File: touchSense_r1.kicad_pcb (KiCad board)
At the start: 2 copper layers, 25 x 25 mm, 13 parts, among them J101 breakout, J102 GS2, J103 GS3, J104 cap/daisy, J105 GS2, U101 AT42QT1010-TSHR

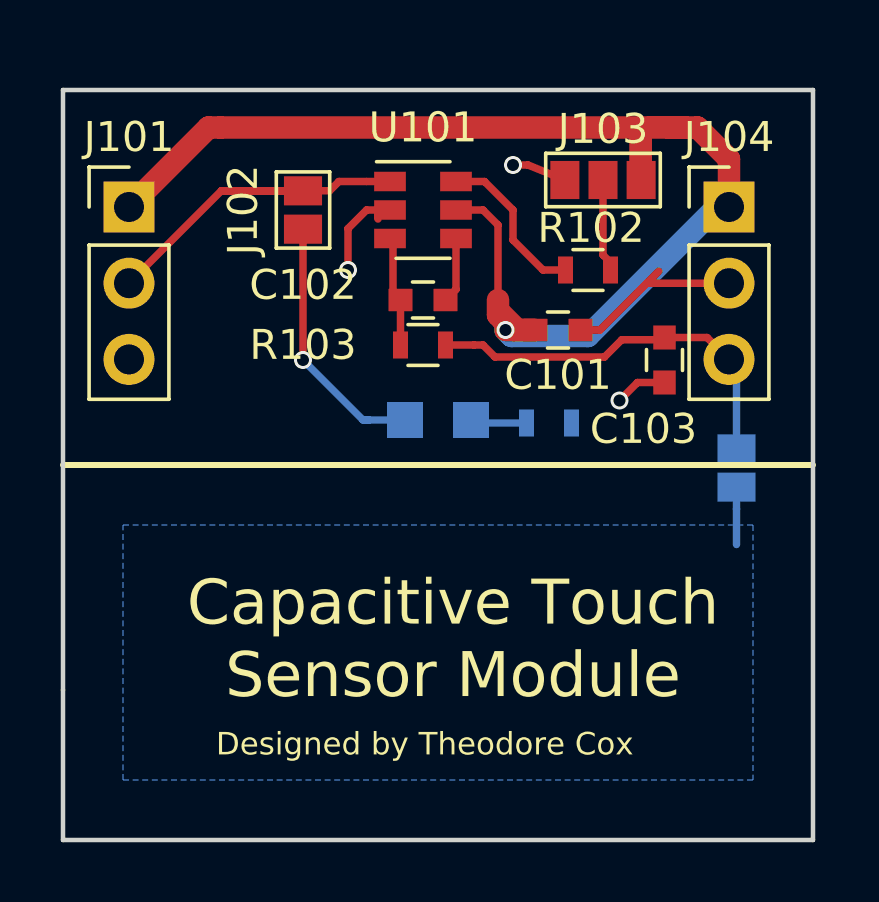
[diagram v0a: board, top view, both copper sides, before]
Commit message: finalized pcblayouts, before uploading to manufacturer
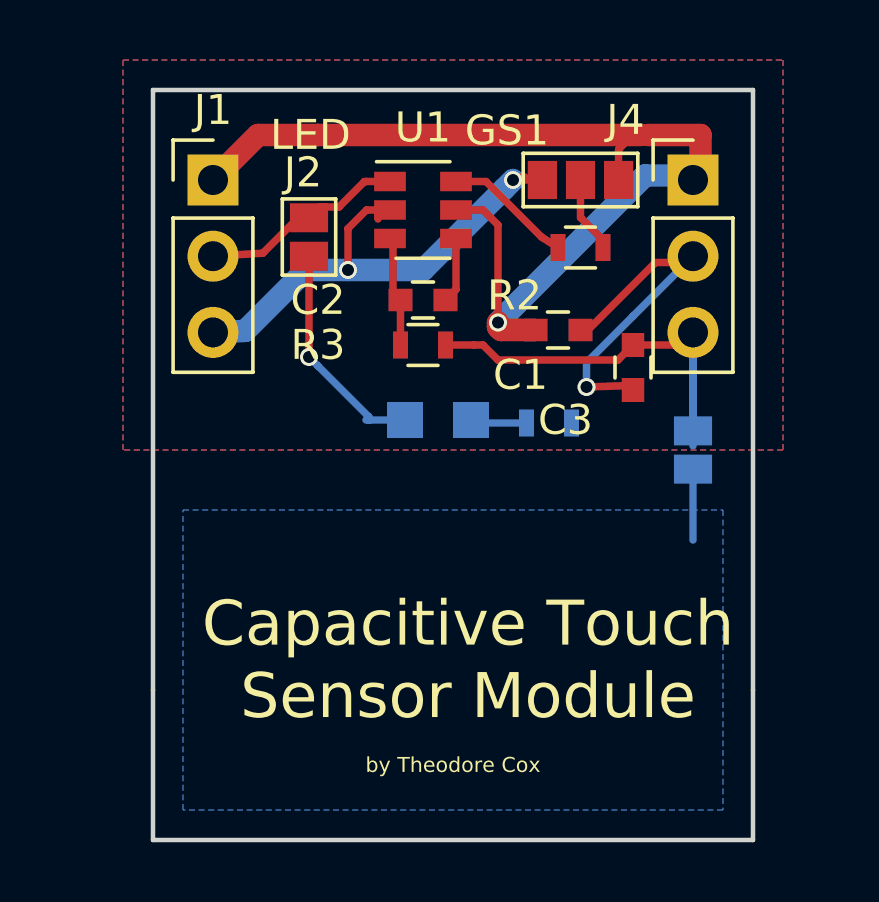
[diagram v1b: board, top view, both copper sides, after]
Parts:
- removed J103: GS3, Connectors:GS3
- added GS1: GS3, Connectors:GS3, F.Cu at (117.2, 103.0)
- added REF***: OSHW-Symbol_13.4x12mm_SilkScreen, Symbols:OSHW-Symbol_13.4x12mm_SilkScreen, B.Cu at (113.0, 119.0)
- moved J1 2.94 mm to (105.0, 103.0)
- moved J3 1.57 mm to (121.0, 112.0)
- moved J4 1.50 mm to (121.0, 103.0)
- moved C3 1.08 mm to (119.0, 109.2)
- moved J2 0.92 mm to (108.2, 104.9)
- moved R2 0.79 mm to (117.2, 105.2)
- renumbered C101 to C1, C102 to C2, C103 to C3, D101 to D1, J101 to J1, J102 to J2, J105 to J3, J104 to J4, R101 to R1, R102 to R2, R103 to R3, U101 to U1
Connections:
- J3 pad 2: (no net) -> /internal
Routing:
- net GND: track 13.9 -> 29.5 mm
- net /VDD: track 48.0 -> 37.6 mm
- net /OUT1: track 14.9 -> 7.88 mm
- net /internal: track 0.00 -> 2.36 mm
- net /CAP_PAD: track 14.2 -> 16.4 mm
- net (no net): track 1.91 -> 0.00 mm
- net Net-(R2-Pad2): track 5.46 -> 4.27 mm
- net Net-(D1-Pad2): track 9.40 -> 8.30 mm
- net Net-(GS1-Pad2): track 3.10 -> 2.56 mm
- added copper zone on B.Cu, net /internal
- removed copper zone on B.Cu, net /CAP_PAD
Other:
- board size 25 x 25 mm -> 20 x 25 mm
- board text added: "LED"
- board text added: "by Theodore Cox"
- board text removed: "Designed by Theodore Cox"

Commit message: new touch implementation
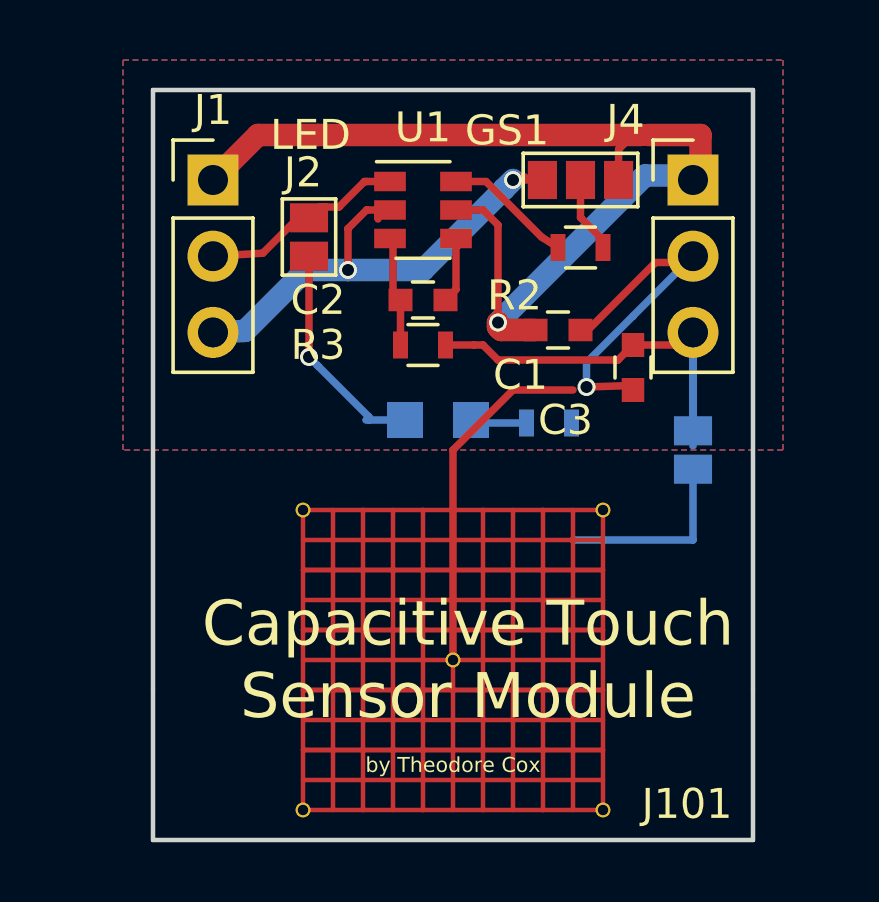
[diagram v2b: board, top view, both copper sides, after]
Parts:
- removed REF***: OSHW-Symbol_13.4x12mm_SilkScreen, Symbols:OSHW-Symbol_13.4x12mm_SilkScreen
- added J101: Hatched_Fill, seniorDesign:HATCHED_FILL_10mm, F.Cu at (113.0, 119.0)
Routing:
- net GND: track 29.5 -> 41.3 mm
- net /internal: track 2.36 -> 6.36 mm

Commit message: organize project folder, small pcb maitenance, generated gerbers
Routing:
- net GND: track 41.3 -> 213.8 mm
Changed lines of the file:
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@@
     (thickness 1.6)
     (drawings 11)
-    (tracks 99)
+    (tracks 144)
     (zones 0)
     (modules 14)
@@
     (user_trace_width 0.75)
     (trace_clearance 0.2)
-    (zone_clearance 0.381)
+    (zone_clearance 0.3)
     (zone_45_only yes)
     (trace_min 0.2)
@@
     (effects (font (size 0.75 0.75) (thickness 0.1875)) (justify right mirror))
   )
+  (segment (start 113 123) (end 119 123) (width 0.25) (layer F.Cu) (net 1))
+  (segment (start 113 122) (end 119 122) (width 0.25) (layer F.Cu) (net 1))
+  (segment (start 113 123) (end 107 123) (width 0.25) (layer F.Cu) (net 1))
+  (segment (start 113 122) (end 107 122) (width 0.25) (layer F.Cu) (net 1))
+  (segment (start 113 121) (end 107 121) (width 0.25) (layer F.Cu) (net 1))
+  (segment (start 113 121) (end 119 121) (width 0.25) (layer F.Cu) (net 1))
+  (segment (start 117.45 109.9) (end 117.1 109.9) (width 0.25) (layer F.Cu) (net 1))
+  (segment (start 115 110) (end 113 112) (width 0.25) (layer F.Cu) (net 1))
+  (segment (start 113 112) (end 113 115) (width 0.25) (layer F.Cu) (net 1))
   (segment (start 117 110) (end 115 110) (width 0.25) (layer F.Cu) (net 1))
-  (segment (start 113 112) (end 113 119) (width 0.25) (layer F.Cu) (net 1) (status 800000))
-  (segment (start 115 110) (end 113 112) (width 0.25) (layer F.Cu) (net 1))
+  (segment (start 117.1 109.9) (end 117 110) (width 0.25) (layer F.Cu) (net 1))
+  (segment (start 113 120) (end 104 120) (width 0.25) (layer F.Cu) (net 1))
+  (segment (start 113 120) (end 119 120) (width 0.25) (layer F.Cu) (net 1))
+  (segment (start 113 119) (end 113 120) (width 0.25) (layer F.Cu) (net 1))
+  (segment (start 113 120) (end 113 121) (width 0.25) (layer F.Cu) (net 1))
+  (segment (start 113 121) (end 113 122) (width 0.25) (layer F.Cu) (net 1))
+  (segment (start 113 122) (end 113 123) (width 0.25) (layer F.Cu) (net 1))
+  (segment (start 113 123) (end 113 124) (width 0.25) (layer F.Cu) (net 1))
+  (segment (start 114 115) (end 120 115) (width 0.25) (layer F.Cu) (net 1))
+  (segment (start 109 119) (end 109 113) (width 0.25) (layer F.Cu) (net 1))
+  (segment (start 110 119) (end 110 113) (width 0.25) (layer F.Cu) (net 1))
+  (segment (start 111 119) (end 111 113) (width 0.25) (layer F.Cu) (net 1))
+  (segment (start 112 119) (end 112 113) (width 0.25) (layer F.Cu) (net 1))
+  (segment (start 113 115) (end 107 115) (width 0.25) (layer F.Cu) (net 1))
+  (segment (start 113 118) (end 107 118) (width 0.25) (layer F.Cu) (net 1))
+  (segment (start 113 118) (end 119 118) (width 0.25) (layer F.Cu) (net 1))
+  (segment (start 117 119) (end 117 113) (width 0.25) (layer F.Cu) (net 1))
+  (segment (start 116 119) (end 116 113) (width 0.25) (layer F.Cu) (net 1))
+  (segment (start 115 119) (end 115 113) (width 0.25) (layer F.Cu) (net 1))
+  (segment (start 114 119) (end 114 115) (width 0.25) (layer F.Cu) (net 1))
+  (segment (start 114 115) (end 114 112) (width 0.25) (layer F.Cu) (net 1))
+  (segment (start 113 117) (end 121 117) (width 0.25) (layer F.Cu) (net 1))
+  (segment (start 113 116) (end 120 116) (width 0.25) (layer F.Cu) (net 1))
+  (segment (start 113 117) (end 106 117) (width 0.25) (layer F.Cu) (net 1))
+  (segment (start 113 116) (end 106 116) (width 0.25) (layer F.Cu) (net 1))
+  (segment (start 113 119) (end 112 119) (width 0.25) (layer F.Cu) (net 1))
+  (segment (start 112 119) (end 111 119) (width 0.25) (layer F.Cu) (net 1))
+  (segment (start 111 119) (end 110 119) (width 0.25) (layer F.Cu) (net 1))
+  (segment (start 110 119) (end 109 119) (width 0.25) (layer F.Cu) (net 1))
+  (segment (start 109 119) (end 106 119) (width 0.25) (layer F.Cu) (net 1))
+  (segment (start 113 119) (end 114 119) (width 0.25) (layer F.Cu) (net 1))
+  (segment (start 114 119) (end 115 119) (width 0.25) (layer F.Cu) (net 1))
+  (segment (start 115 119) (end 116 119) (width 0.25) (layer F.Cu) (net 1))
+  (segment (start 116 119) (end 117 119) (width 0.25) (layer F.Cu) (net 1))
+  (segment (start 117 119) (end 120 119) (width 0.25) (layer F.Cu) (net 1))
+  (segment (start 113 115) (end 113 116) (width 0.25) (layer F.Cu) (net 1))
+  (segment (start 113 116) (end 113 117) (width 0.25) (layer F.Cu) (net 1))
+  (segment (start 113 117) (end 113 118) (width 0.25) (layer F.Cu) (net 1))
+  (segment (start 113 118) (end 113 119) (width 0.25) (layer F.Cu) (net 1))
   (segment (start 112 106) (end 114.700001 103.299999) (width 0.75) (layer B.Cu) (net 1))
   (segment (start 109.5 106) (end 112 106) (width 0.75) (layer B.Cu) (net 1))
@@
   (segment (start 111 105.05) (end 110.9 104.95) (width 0.25) (layer F.Cu) (net 7) (status 30))
   (segment (start 111.25 108.5) (end 111.25 107) (width 0.25) (layer F.Cu) (net 7) (status 10))
-  (segment (start 108.499999 109.199999) (end 108.2 108.9) (width 0.25) (layer B.Cu) (net 8))
-  (segment (start 110.2 111) (end 110.2 110.9) (width 0.25) (layer B.Cu) (net 8))
+  (segment (start 108.2 108.9) (end 108.2 109.2) (width 0.25) (layer B.Cu) (net 8))
+  (via (at 108.2 108.9) (size 0.6) (drill 0.4) (layers F.Cu B.Cu) (net 8))
   (segment (start 108.2 105.54) (end 108.2 108.9) (width 0.25) (layer F.Cu) (net 8))
-  (segment (start 110.2 110.9) (end 108.499999 109.199999) (width 0.25) (layer B.Cu) (net 8))
-  (via (at 108.2 108.9) (size 0.6) (drill 0.4) (layers F.Cu B.Cu) (net 8))
+  (segment (start 110 111) (end 111.4 111) (width 0.25) (layer B.Cu) (net 8) (status 800000))
+  (segment (start 108.2 109.2) (end 110 111) (width 0.25) (layer B.Cu) (net 8))
+  (segment (start 111.25 110.85) (end 111.4 111) (width 0.25) (layer B.Cu) (net 8))
   (segment (start 108.56 105.54) (end 108.2 105.54) (width 0.25) (layer F.Cu) (net 8) (status 30))
-  (segment (start 110.1 111) (end 110.2 111) (width 0.25) (layer B.Cu) (net 8))
-  (segment (start 110.2 111) (end 111.75 111) (width 0.25) (layer B.Cu) (net 8))
   (segment (start 115.45 111.1) (end 113.7 111.1) (width 0.25) (layer B.Cu) (net 9))
   (segment (start 113.7 111.1) (end 113.6 111) (width 0.25) (layer B.Cu) (net 9))
@@
     (polygon
       (pts
-        (xy 124 112) (xy 102 112) (xy 102 99) (xy 124 99)
+        (xy 124 112) (xy 123 112) (xy 123 125) (xy 103 125) (xy 103 112)
+        (xy 102 112) (xy 102 99) (xy 124 99)
       )
     )
